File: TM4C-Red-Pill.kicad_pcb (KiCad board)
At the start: 2 copper layers, 21.5 x 59.4 mm, 34 parts, among them IC1 TM4C123GH6PMI7R, J1 Conn_01x22, J2 Conn_01x22, J3 Conn_02x05_Odd_Even, J4 USB_C_Receptacle_USB2.0_16P, U1 TLV75533PDBV, U2 USBLC6-2SC6, Y1 ABM3-16.000MHZ-B2-T, Y2 ABS07-32.768KHZ-T

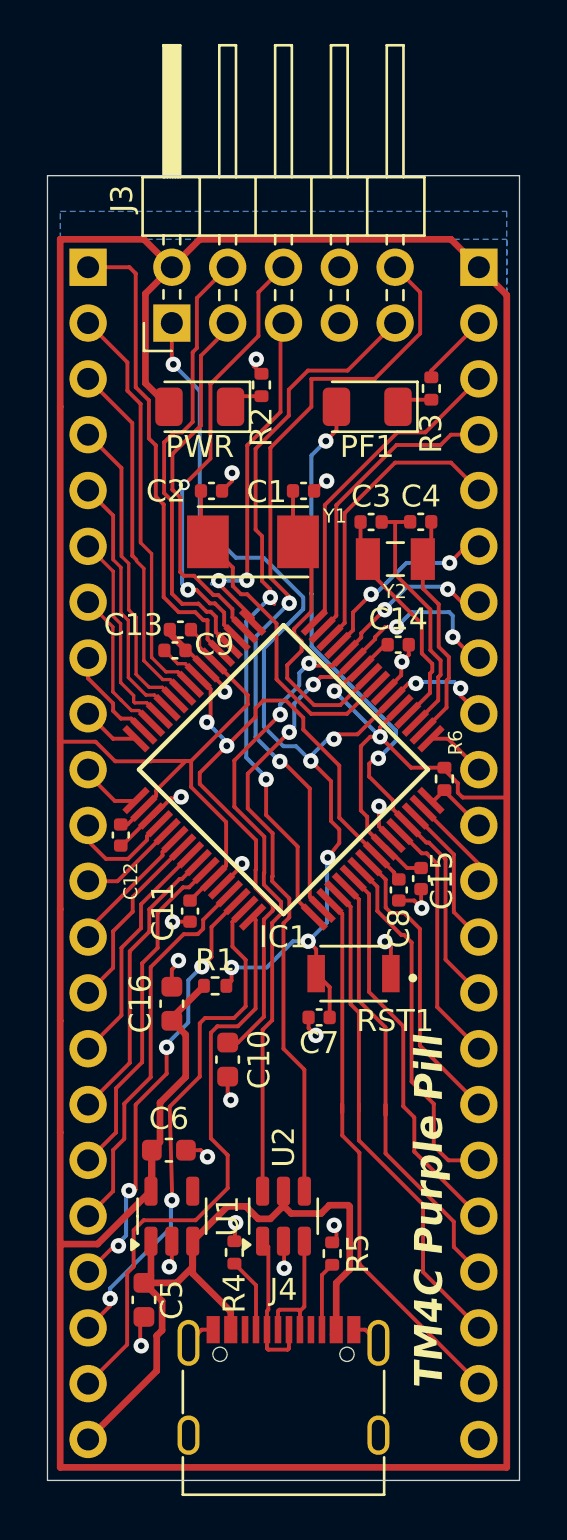
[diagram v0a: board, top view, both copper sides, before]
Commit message: Renamed project to TM4C Red Pill
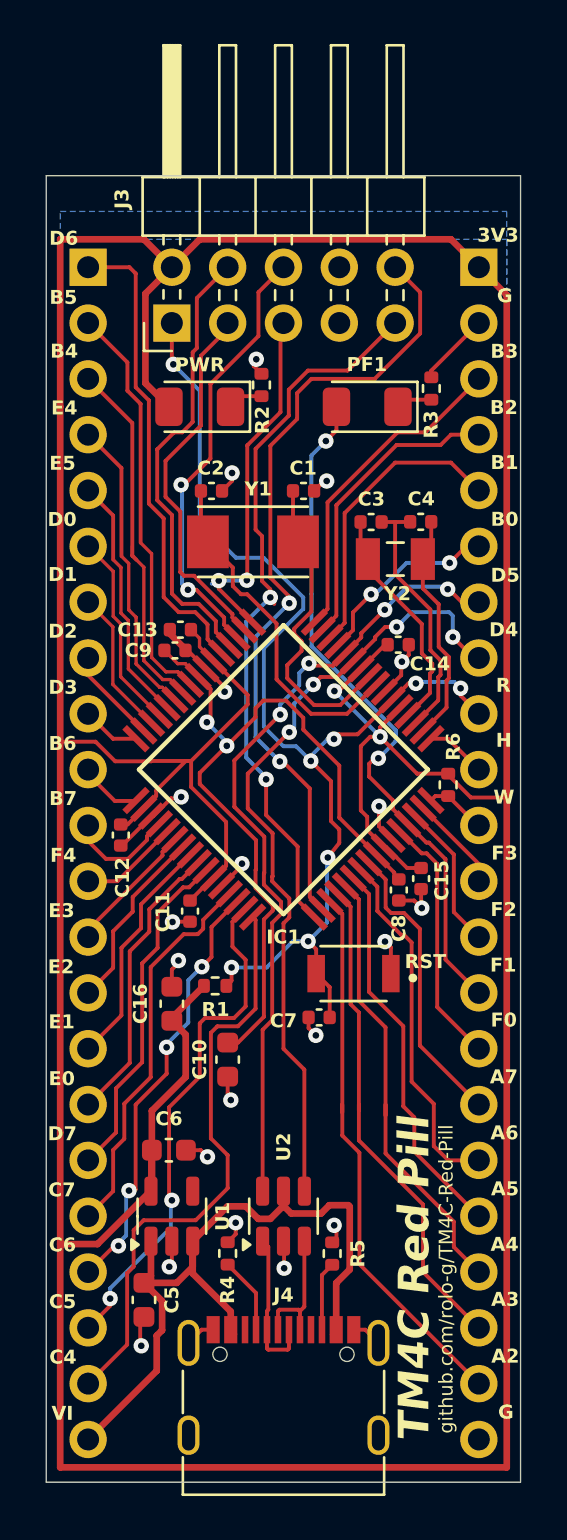
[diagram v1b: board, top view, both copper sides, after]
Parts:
- moved R6 0.32 mm to (143.4, 99.8)
- moved R4 0.31 mm to (133.3, 121.1)
- renumbered RST1 to RST
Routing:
- net /PB4: track 16.2 -> 16.9 mm
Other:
- board size 21.5 x 59.4 mm -> 21.6 x 59.4 mm
- board text added: "3V3"
- board text added: "A2"
- board text added: "A3"
- board text added: "A4"
- board text added: "A5"
- board text added: "A6"
- board text added: "A7"
- board text added: "B0"
- board text added: "B1"
- board text added: "B2"
- board text added: "B3"
- board text added: "B4"
- board text added: "B5"
- board text added: "B6"
- board text added: "B7"
- board text added: "C4"
- board text added: "C5"
- board text added: "C6"
- board text added: "C7"
- board text added: "D0"
- board text added: "D1"
- board text added: "D2"
- board text added: "D3"
- board text added: "D4"
- board text added: "D5"
- board text added: "D6"
- board text added: "D7"
- board text added: "E0"
- board text added: "E1"
- board text added: "E2"
- board text added: "E3"
- board text added: "E4"
- board text added: "E5"
- board text added: "F0"
- board text added: "F1"
- board text added: "F2"
- board text added: "F3"
- board text added: "F4"
- board text added: "G"
- board text added: "H"
- board text added: "R"
- board text added: "Rev 0.3 Created by Rolando Rosales github.com/rolo-g/TM4C-Red-Pill Notes: Max regulator current is 500mA"
- board text added: "TM4C Red Pill"
- board text added: "VI"
- board text added: "W"
- board text added: "github.com/rolo-g/TM4C-Red-Pill"
- board text removed: "TM4C Purple Pill"
